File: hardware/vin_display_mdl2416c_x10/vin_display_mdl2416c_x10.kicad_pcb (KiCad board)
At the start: 2 copper layers, 221 x 83.8 mm, 61 parts, among them J1 DEBUG, J2 USB_B_Micro, J3 DEBUG_UART, J4 IF_UART, J5 AUX_CONNECTOR, Q1 BSS138, SW1 SW_RESET, SW2 BOOTSEL, SW3 KNOB, U1 W25Q16JVSNIQ, U10 MDL2416C, U11 MDL2416C, U12 MDL2416C, U13 MDL2416C, U14 MDL2416C, U2 MIC23050-SYML, U3 RP2040, U4 HEF4028BT, U5 MDL2416C, U6 MDL2416C, U7 MDL2416C, U8 MDL2416C, U9 MDL2416C, X1 12MHz

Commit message: work on pcb layout
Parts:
- J4: value IF_UART -> Conn_01x04; footprint Connector_PinHeader_2.54mm:PinHeader_1x03_P2.54mm_Vertical -> Connector_PinHeader_2.54mm:PinHeader_1x04_P2.54mm_Vertical
- moved SW2 119.2 mm to (175.0, 95.0)
- moved R1 103.3 mm to (177.5, 91.2), turned to 180 degrees
- moved SW1 103.2 mm to (161.1, 95.0)
- moved R10 67.2 mm to (47.2, 61.0), turned to 90 degrees
- moved R6 62.8 mm to (48.8, 61.0), turned to 90 degrees
- moved Q1 59.6 mm to (43.7, 69.6), turned to -90 degrees
- moved C15 56.2 mm to (48.0, 58.7), turned to 180 degrees
- moved D2 54.3 mm to (30.0, 69.3), turned to -90 degrees
- moved R5 53.8 mm to (43.7, 66.5)
- moved R9 50.7 mm to (47.0, 75.4), turned to 90 degrees
- moved C17 50.3 mm to (47.8, 73.1), turned to 180 degrees
- moved R11 49.1 mm to (44.2, 75.4), turned to 90 degrees
- moved R12 48.1 mm to (42.7, 75.4), turned to -90 degrees
- moved C14 46.2 mm to (36.3, 85.6), turned to 180 degrees
- moved C6 45.6 mm to (36.3, 91.9), turned to 180 degrees
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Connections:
- net Net-(R2-Pad2) renamed USB_D+
- net Net-(R3-Pad2) renamed USB_D-
- C1 pad 1: Net-(C1-Pad1) -> 3V3
- C2 pad 1: Net-(C1-Pad1) -> 3V3
- J4 pad 1: UART1_TX -> VSYS
- J4 pad 2: GND -> UART1_TX
- J4 pad 3: UART1_RX -> GND
- U1 pad 8: Net-(C1-Pad1) -> 3V3
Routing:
- net DISP_WR: track 0.00 -> 304.0 mm, vias 0 -> 20
- net DISP_CLR: track 0.00 -> 301.1 mm, vias 0 -> 16
- net DISP_CUE: track 0.00 -> 298.5 mm, vias 0 -> 16
- net DISP_CU: track 0.00 -> 293.7 mm, vias 0 -> 16
- net DISP_A0: track 0.00 -> 293.1 mm, vias 0 -> 2
- net DISP_BL: track 0.00 -> 279.2 mm, vias 0 -> 16
- net DISP_D4: track 0.00 -> 273.3 mm, vias 0 -> 16
- net DISP_D5: track 0.00 -> 268.0 mm, vias 0 -> 16
- net DISP_D6: track 0.00 -> 262.8 mm, vias 0 -> 16
- net DISP_D3: track 0.00 -> 257.5 mm, vias 0 -> 16
- net DISP_D2: track 0.00 -> 252.6 mm, vias 0 -> 16
- net DISP_D0: track 0.00 -> 237.4 mm
- net DISP_A1: track 0.00 -> 231.2 mm, vias 0 -> 16
- net VSYS: track 0.00 -> 194.1 mm, vias 0 -> 1
- net DISP_D1: track 0.00 -> 185.6 mm, vias 0 -> 12
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- added copper zone on F.Cu, net 3V3
- added copper zone on B.Cu, net GND
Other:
- board size 221 x 83.8 mm -> 178.8 x 53.1 mm

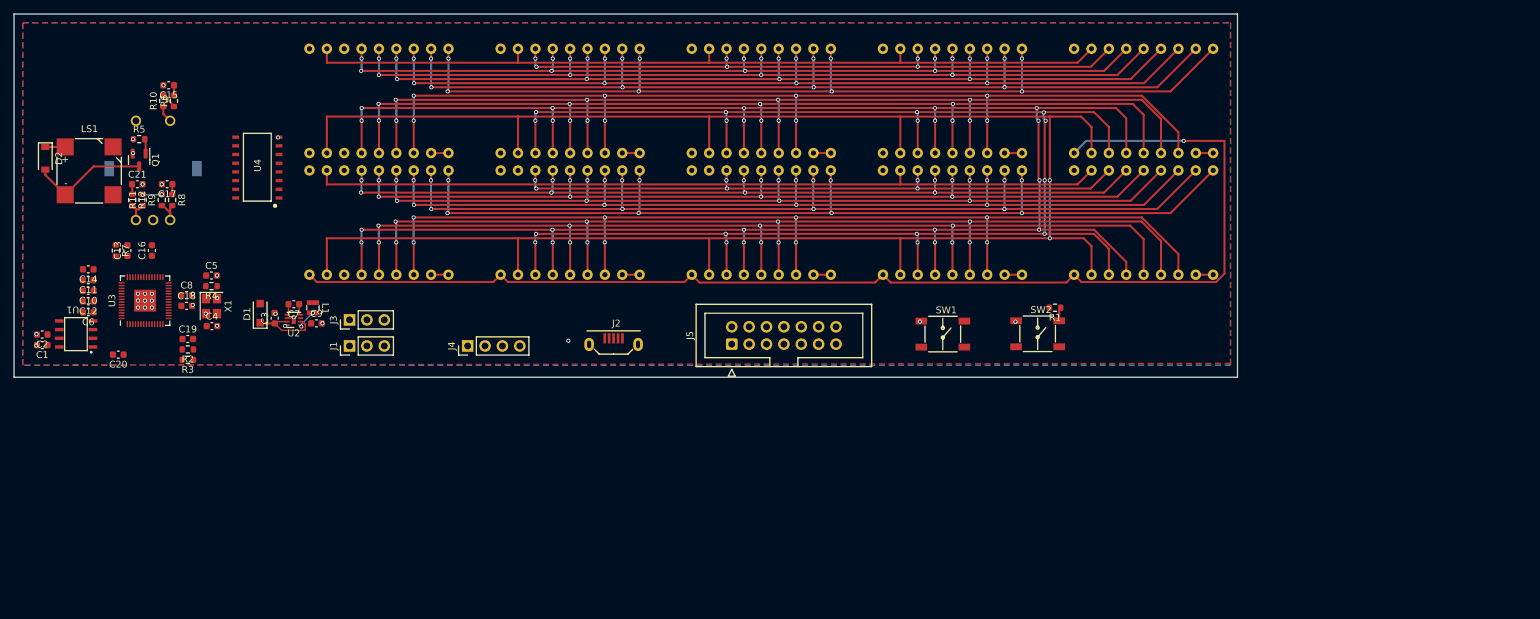
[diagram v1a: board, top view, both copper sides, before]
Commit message: mdl2416c_x10 pcb routed
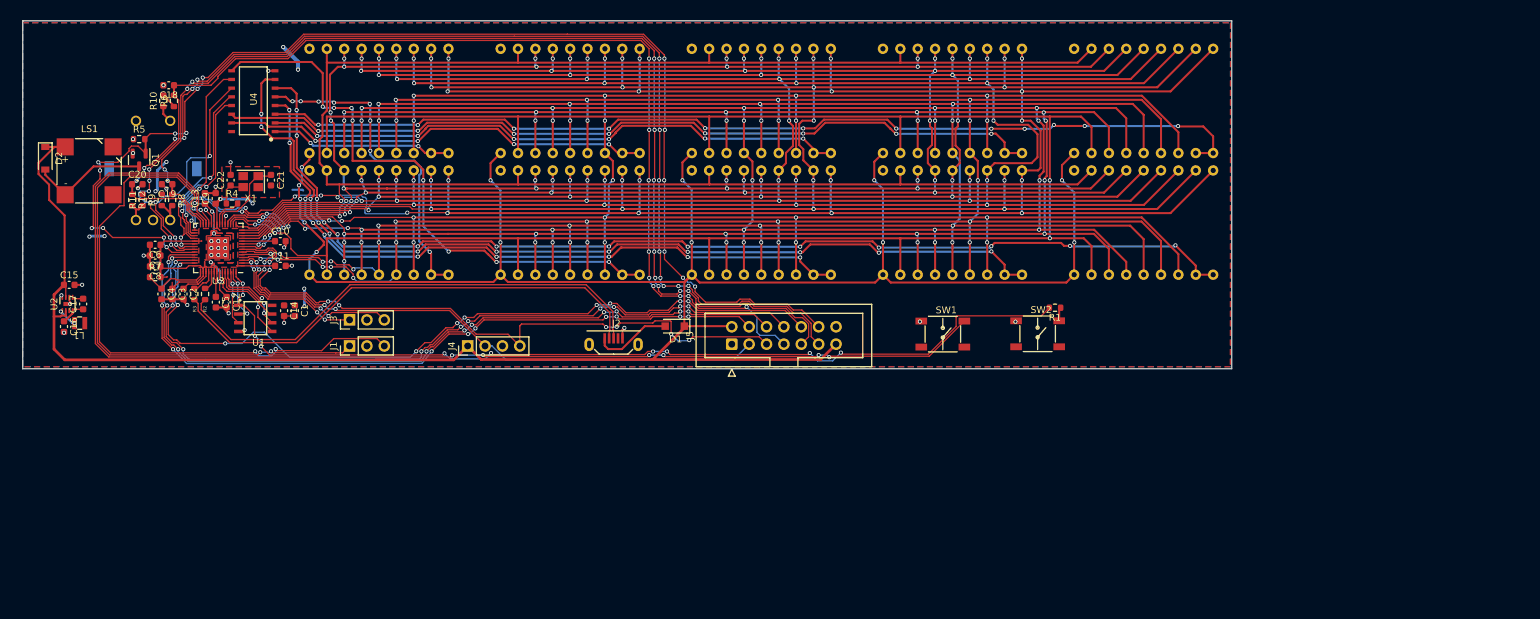
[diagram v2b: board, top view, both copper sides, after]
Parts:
- added C11: 100n, Capacitor_SMD:C_0603_1608Metric, F.Cu at (64.3, 85.1)
- moved D1 60.6 mm to (122.0, 93.9), turned to 180 degrees
- moved C1 37.3 mm to (66.4, 91.6), turned to -90 degrees
- moved C16 36.9 mm to (32.7, 93.9), turned to -90 degrees
- moved C14 35.5 mm to (64.9, 91.6), turned to -90 degrees
- moved L1 34.2 mm to (35.0, 93.4), turned to 180 degrees
- moved U2 33.2 mm to (33.2, 90.6), turned to 90 degrees
- moved C17 30.8 mm to (35.5, 90.6), turned to 90 degrees
- moved C15 30.4 mm to (33.5, 87.8), turned to 0 degrees
- moved C10 28.9 mm to (64.3, 81.5), turned to 0 degrees
- moved C21 23.0 mm to (62.9, 72.5), turned to -90 degrees
- moved U1 22.1 mm to (58.2, 90.8), turned to -90 degrees
- moved C9 20.9 mm to (54.9, 75.2), turned to 90 degrees
- moved C12 20.3 mm to (56.5, 90.4), turned to -90 degrees
- moved X1 19.1 mm to (60.0, 72.8), turned to 180 degrees
- moved C5 18.6 mm to (54.9, 90.4), turned to -90 degrees
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- renumbered C20 to C10, C6 to C12, C8 to C13, C2 to C14, C3 to C15, C9 to C16, C7 to C17, C15 to C18, C17 to C19, C10 to C2, C21 to C20, C4 to C21, C5 to C22, C11 to C3, C14 to C4, C12 to C5, C13 to C6, C16 to C7, C18 to C8, C19 to C9
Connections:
- net USB_DM renamed USB_DN
- U3 pad 27: DISP_CUE -> ENC_A
- U3 pad 28: DISP_CU -> ENC_B
- U3 pad 4: ENC_A -> DISP_CUE
- U3 pad 5: ENC_B -> DISP_CU
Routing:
- net VSYS: track 194.1 -> 392.2 mm, vias 1 -> 13
- net SPEAKER: track 2.16 -> 182.4 mm, vias 0 -> 16
- net Net-(U3-RUN): track 0.00 -> 175.9 mm, vias 0 -> 6
- net ENC_B: track 1.48 -> 168.5 mm, vias 0 -> 14
- net KNOB_SW: track 1.47 -> 165.3 mm, vias 0 -> 15
- net ENC_A: track 1.49 -> 161.0 mm, vias 0 -> 12
- net DISP6_CE: track 2.54 -> 161.1 mm, vias 0 -> 14
- net DISP1_CE: track 2.54 -> 146.7 mm, vias 0 -> 12
- net DISP7_CE: track 2.54 -> 138.1 mm, vias 0 -> 12
- net Net-(U1-CS): track 0.00 -> 135.3 mm, vias 0 -> 10
- net DISP2_CE: track 2.54 -> 122.6 mm, vias 0 -> 8
- net GP29: track 0.00 -> 114.8 mm, vias 0 -> 10
- net GP28: track 0.00 -> 112.7 mm, vias 0 -> 10
- net GP27: track 0.00 -> 110.4 mm, vias 0 -> 10
- net GP26: track 0.00 -> 107.5 mm, vias 0 -> 10
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- added copper zone on F.Cu, net 1V1
- added copper zone on F.Cu, net GND
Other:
- board size 178.8 x 53.1 mm -> 176.7 x 50.9 mm

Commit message: mdl2416c_x10 pcb fixes/adjustments
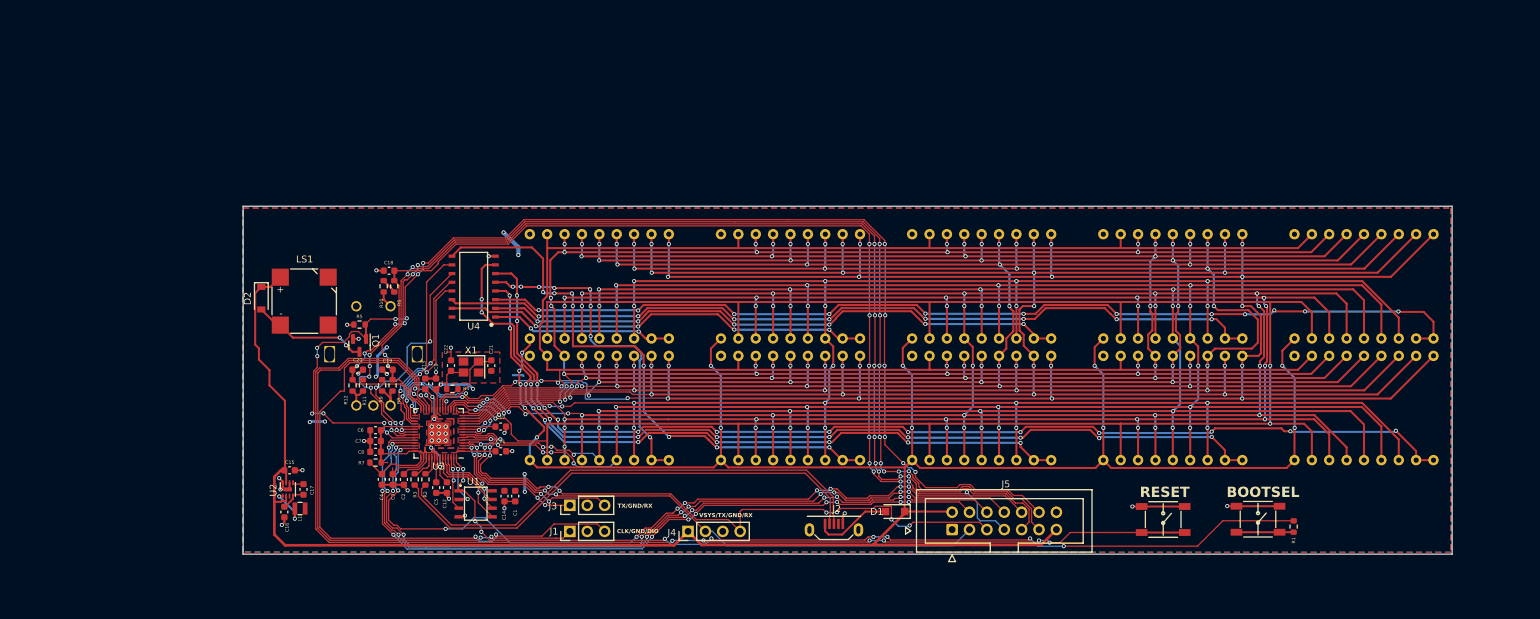
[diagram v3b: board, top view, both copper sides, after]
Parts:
- moved R1 47.3 mm to (212.4, 123.2), turned to 90 degrees
- moved J5 42.1 mm to (162.5, 123.6)
- moved SW2 42.1 mm to (207.2, 122.1)
- moved U10 42.1 mm to (222.7, 105.8)
- moved U11 42.1 mm to (194.8, 105.8)
- moved U12 42.1 mm to (166.8, 105.8)
- moved U13 42.1 mm to (138.9, 105.8)
- moved U14 42.1 mm to (110.9, 105.8)
- moved C17 42.1 mm to (67.7, 117.7)
- moved C18 42.1 mm to (80.2, 85.8)
- moved C20 42.1 mm to (75.6, 100.2)
- moved C3 42.1 mm to (80.8, 116.3)
- moved C9 42.1 mm to (87.1, 102.3)
- moved R4 42.1 mm to (89.5, 103.1)
- moved R6 42.1 mm to (81.0, 88.1)
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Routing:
- net GND: track 29.9 -> 52.5 mm
- net Net-(R1-Pad1): track 1.70 -> 8.36 mm
- net VSYS: track 392.2 -> 398.1 mm
- net Net-(U2-SW): track 2.98 -> 6.22 mm
- net Net-(U3-RUN): track 175.9 -> 174.6 mm
- net Net-(D2-A): track 17.4 -> 18.6 mm, vias 0 -> 2
- net Net-(U1-CS): track 135.3 -> 136.1 mm
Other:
- board text added: "BOOTSEL"
- board text added: "CLK/GND/DIO"
- board text added: "CoolHorse Industries 2023"
- board text added: "RESET"
- board text added: "TX/GND/RX"
- board text added: "VSYS/TX/GND/RX"
- board text added: "VinDisplay mdl2416c_x10 v1.0"

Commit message: minor schematic fixes
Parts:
- C21, C22: value 15p -> 19p
- J4: value Conn_01x04 -> IF_UART
- moved C1 8.19 mm to (106.6, 116.7)
- moved C10 8.19 mm to (104.5, 106.6)
- moved C11 8.19 mm to (104.5, 110.2)
- moved C12 8.19 mm to (96.6, 115.5)
- moved C13 8.19 mm to (93.5, 100.3)
- moved C17 8.19 mm to (75.7, 115.8)
- moved C2 8.19 mm to (90.3, 114.3)
- moved C20 8.19 mm to (83.6, 98.3)
- moved C21 8.19 mm to (103.1, 97.7)
- moved C5 8.19 mm to (95.1, 115.5)
- moved C7 8.19 mm to (86.2, 108.7)
- moved J4 8.19 mm to (131.9, 121.9)
- moved R10 8.19 mm to (87.4, 86.1)
- moved R12 8.19 mm to (82.8, 100.6)
- moved R4 8.19 mm to (97.4, 101.1)
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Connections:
- SW3 pad G: GND -> (no net)
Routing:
- net GP29: track 114.8 -> 112.6 mm, vias 10 -> 4
- net GP28: track 112.7 -> 110.6 mm, vias 10 -> 4
- net GP27: track 110.4 -> 109.2 mm, vias 10 -> 4
- net USB_DP: track 72.6 -> 73.8 mm, vias 0 -> 4
- net VSYS: track 398.1 -> 399.2 mm, vias 13 -> 15
- net SPEAKER: track 182.3 -> 183.4 mm
- net KNOB_SW: track 165.3 -> 166.3 mm, vias 15 -> 13
- net 3V3: track 72.7 -> 71.8 mm
- net USB_DN: track 72.6 -> 73.1 mm, vias 0 -> 4
- net ENC_B: track 168.5 -> 168.9 mm, vias 14 -> 12
- net UART0_RX: track 27.7 -> 27.2 mm, vias 4 -> 2
- net ENC_A: track 161.0 -> 160.5 mm, vias 12 -> 10
- net UART1_RX: track 95.9 -> 95.7 mm, vias 8 -> 6
- net GP26: track 107.5 -> 107.6 mm, vias 10 -> 4
- net UART0_TX: vias 4 -> 2
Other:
- board size 176.7 x 50.9 mm -> 176 x 50 mm

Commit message: update schematic; add pdf
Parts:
- R10: value 10K -> 1K
- U4: value HEF4028BT -> SN74HC42D
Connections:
- R10 pad 2: 3V3 -> KNOB_SW
- U4 pad 1: DISP5_CE -> DISP1_CE
- U4 pad 10: DISP_CE_A0 -> DISP9_CE
- U4 pad 11: DISP_CE_A3 -> DISP10_CE
- U4 pad 12: DISP_CE_A2 -> DISP_CE_A3
- U4 pad 13: DISP_CE_A1 -> DISP_CE_A2
- U4 pad 14: DISP2_CE -> DISP_CE_A1
- U4 pad 15: DISP4_CE -> DISP_CE_A0
- U4 pad 2: DISP3_CE -> DISP2_CE
- U4 pad 3: DISP1_CE -> DISP3_CE
- U4 pad 4: DISP8_CE -> DISP4_CE
- U4 pad 5: DISP10_CE -> DISP5_CE
- U4 pad 9: DISP9_CE -> DISP8_CE
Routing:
- net DISP8_CE: track 102.6 -> 113.5 mm, vias 10 -> 8
- net DISP5_CE: track 26.6 -> 37.2 mm
- net DISP10_CE: track 49.0 -> 57.4 mm, vias 8 -> 6
- net DISP3_CE: track 86.3 -> 93.3 mm
- net DISP_CE_A0: track 27.3 -> 20.9 mm, vias 2 -> 4
- net 3V3: track 71.8 -> 76.0 mm, vias 10 -> 14
- net DISP6_CE: track 161.1 -> 165.3 mm, vias 14 -> 12
- net DISP7_CE: track 138.1 -> 134.0 mm
- net DISP1_CE: track 146.7 -> 150.1 mm
- net DISP4_CE: track 62.9 -> 60.4 mm
- net VSYS: track 399.2 -> 397.1 mm
- net Net-(D2-A): track 18.6 -> 16.5 mm
- net DISP9_CE: track 85.2 -> 83.3 mm
- net DISP_CE_A1: track 25.1 -> 23.3 mm
- net KNOB_SW: track 166.3 -> 167.8 mm
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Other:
- board text added: "VinDisplay mdl2416c_x10 v1.1"
- board text removed: "VinDisplay mdl2416c_x10 v1.0"

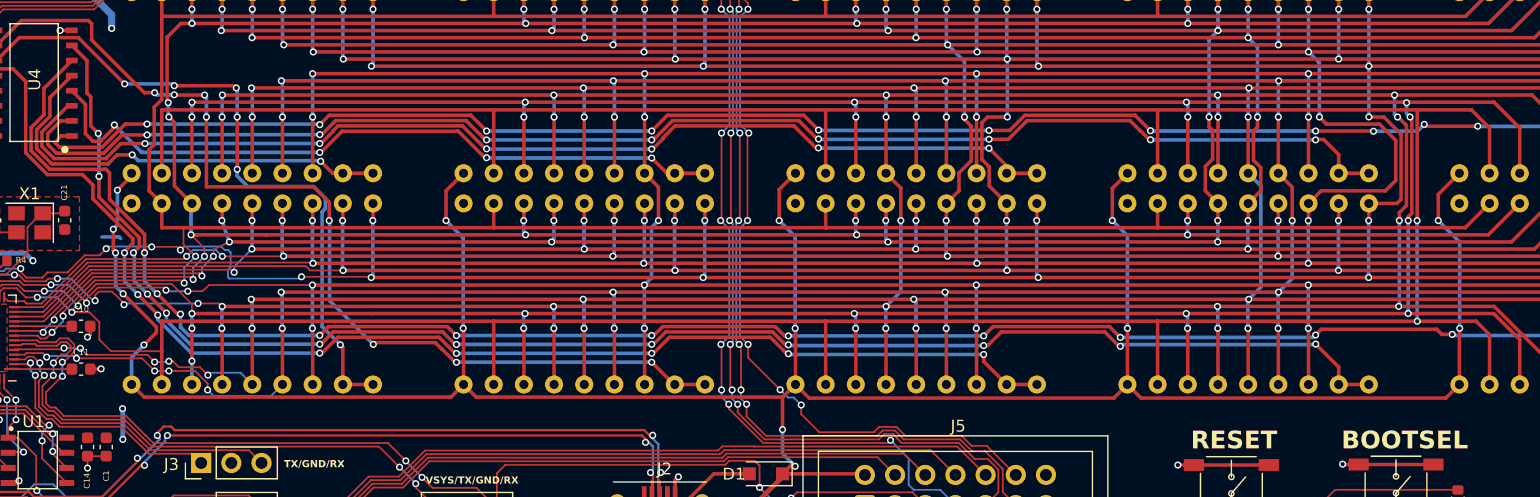
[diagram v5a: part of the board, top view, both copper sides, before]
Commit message: minor pcb changes; add decoupling caps in mdl2416c_x10
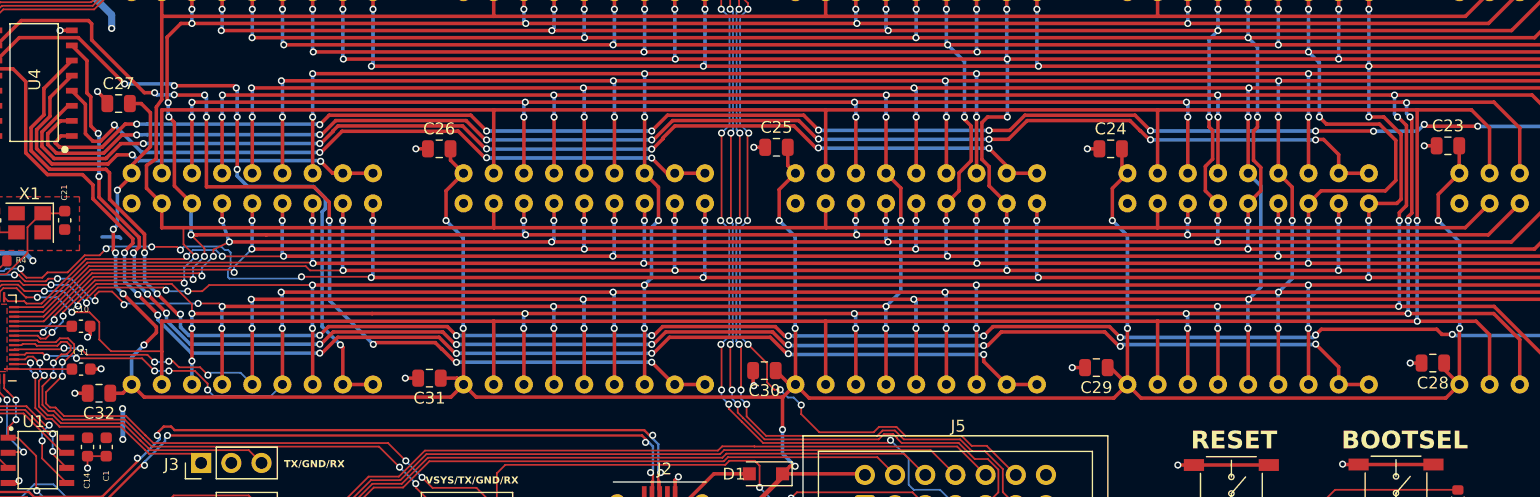
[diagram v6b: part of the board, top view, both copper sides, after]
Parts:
- added C23: 4.7uF, Capacitor_SMD:C_0805_2012Metric, F.Cu at (219.5, 91.4)
- added C24: 4.7uF, Capacitor_SMD:C_0805_2012Metric, F.Cu at (191.1, 91.6)
- added C25: 4.7uF, Capacitor_SMD:C_0805_2012Metric, F.Cu at (163.0, 91.5)
- added C26: 4.7uF, Capacitor_SMD:C_0805_2012Metric, F.Cu at (134.6, 91.6)
- added C27: 4.7uF, Capacitor_SMD:C_0805_2012Metric, F.Cu at (107.6, 87.8)
- added C28: 4.7uF, Capacitor_SMD:C_0805_2012Metric, F.Cu at (218.3, 109.7)
- added C29: 4.7uF, Capacitor_SMD:C_0805_2012Metric, F.Cu at (189.9, 110.1)
- added C30: 4.7uF, Capacitor_SMD:C_0805_2012Metric, F.Cu at (162.0, 110.3)
- added C31: 4.7uF, Capacitor_SMD:C_0805_2012Metric, F.Cu at (133.8, 110.9)
- added C32: 4.7uF, Capacitor_SMD:C_0805_2012Metric, F.Cu at (106.0, 112.2)
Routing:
- net VSYS: track 397.1 -> 425.4 mm
- net GND: track 52.4 -> 63.3 mm, vias 32 -> 42
